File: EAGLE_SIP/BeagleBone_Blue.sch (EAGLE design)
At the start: 265 parts, among them M1 JST_ZH_2, M2 JST_ZH_2, M3 JST_ZH_2, M4 JST_ZH_2, P10 SCHA5B0200, Q3 MOSFET-N, U1 TPD4S012_DRY_6, U4 TPD4S012_DRY_6, U5 24LC_32AT-I/OT, U6 SN74LVC1G07_DCK_5, U7 TPS2051B_D_8, U8 MTFC4GLDEA, Y1 CM200C-32.768KAZF-UT, Y2 445C33D24M00000

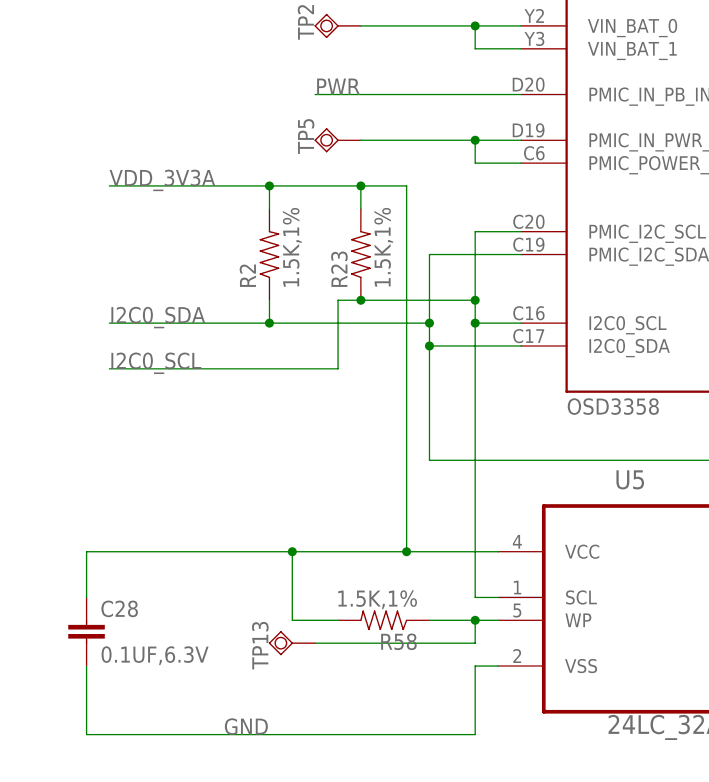
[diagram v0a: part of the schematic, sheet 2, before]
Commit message: Move U5 from VDD_3V3A to 3.3V
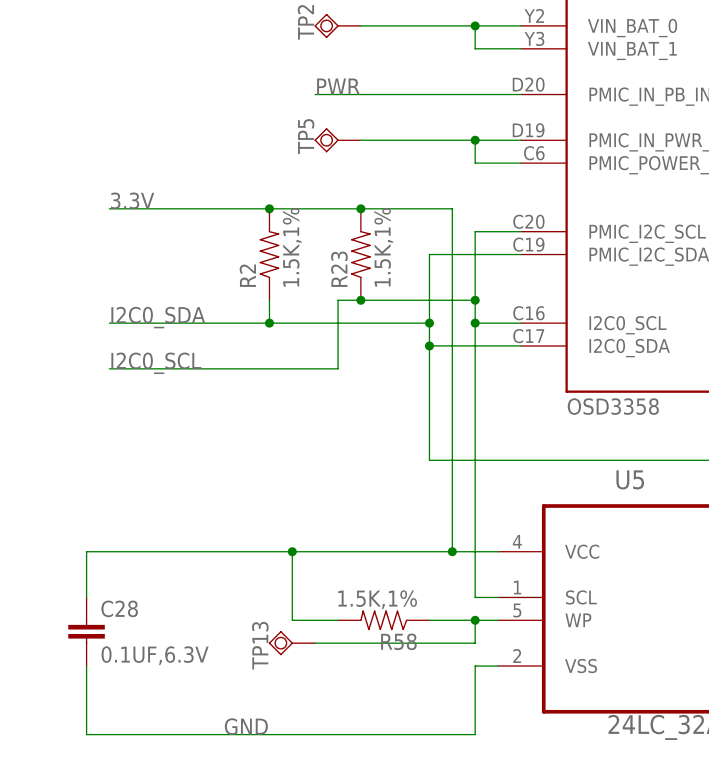
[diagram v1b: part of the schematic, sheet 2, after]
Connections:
- net 3.3V: now also C28.1, R2.2, R23.2, R58.2, U5.VCC
- net VDD_3V3A: no longer C28.1, R2.2, R23.2, R58.2, U5.VCC
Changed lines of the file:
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@@
 <net name="VDD_3V3A" class="0">
-<segment>
-<pinref part="R2" gate="G$1" pin="2"/>
-<wire x1="38.1" y1="203.2" x2="38.1" y2="205.74" width="0.1524" layer="91"/>
-<wire x1="20.32" y1="205.74" x2="38.1" y2="205.74" width="0.1524" layer="91"/>
-<pinref part="R23" gate="G$1" pin="2"/>
-<wire x1="38.1" y1="205.74" x2="48.26" y2="205.74" width="0.1524" layer="91"/>
-<wire x1="48.26" y1="205.74" x2="48.26" y2="203.2" width="0.1524" layer="91"/>
-<junction x="38.1" y="205.74"/>
-<label x="20.32" y="205.74" size="1.778" layer="95"/>
-<wire x1="48.26" y1="205.74" x2="53.34" y2="205.74" width="0.1524" layer="91"/>
-<junction x="48.26" y="205.74"/>
-<wire x1="53.34" y1="205.74" x2="53.34" y2="165.1" width="0.1524" layer="91"/>
-<pinref part="U5" gate="A" pin="VCC"/>
-<wire x1="53.34" y1="165.1" x2="63.5" y2="165.1" width="0.1524" layer="91"/>
-<wire x1="53.34" y1="165.1" x2="40.64" y2="165.1" width="0.1524" layer="91"/>
-<junction x="53.34" y="165.1"/>
-<wire x1="40.64" y1="165.1" x2="40.64" y2="157.48" width="0.1524" layer="91"/>
-<pinref part="R58" gate="G$1" pin="2"/>
-<wire x1="40.64" y1="157.48" x2="45.72" y2="157.48" width="0.1524" layer="91"/>
-<pinref part="C28" gate="G$1" pin="1"/>
-<wire x1="40.64" y1="165.1" x2="17.78" y2="165.1" width="0.1524" layer="91"/>
-<wire x1="17.78" y1="165.1" x2="17.78" y2="160.02" width="0.1524" layer="91"/>
-<junction x="40.64" y="165.1"/>
-</segment>
 <segment>
 <pinref part="R60" gate="G$1" pin="2"/>
@@
 <label x="236.22" y="210.82" size="1.778" layer="95"/>
 </segment>
+<segment>
+<pinref part="R58" gate="G$1" pin="2"/>
+<wire x1="40.64" y1="157.48" x2="45.72" y2="157.48" width="0.1524" layer="91"/>
+<pinref part="U5" gate="A" pin="VCC"/>
+<pinref part="C28" gate="G$1" pin="1"/>
+<wire x1="63.5" y1="165.1" x2="58.42" y2="165.1" width="0.1524" layer="91"/>
+<wire x1="58.42" y1="165.1" x2="40.64" y2="165.1" width="0.1524" layer="91"/>
+<wire x1="40.64" y1="165.1" x2="17.78" y2="165.1" width="0.1524" layer="91"/>
+<wire x1="17.78" y1="165.1" x2="17.78" y2="160.02" width="0.1524" layer="91"/>
+<wire x1="58.42" y1="165.1" x2="58.42" y2="203.2" width="0.1524" layer="91"/>
+<junction x="58.42" y="165.1"/>
+<pinref part="R23" gate="G$1" pin="2"/>
+<wire x1="58.42" y1="203.2" x2="48.26" y2="203.2" width="0.1524" layer="91"/>
+<pinref part="R2" gate="G$1" pin="2"/>
+<wire x1="38.1" y1="203.2" x2="48.26" y2="203.2" width="0.1524" layer="91"/>
+<junction x="48.26" y="203.2"/>
+<wire x1="38.1" y1="203.2" x2="20.32" y2="203.2" width="0.1524" layer="91"/>
+<junction x="38.1" y="203.2"/>
+<label x="20.32" y="203.2" size="1.778" layer="95"/>
+<wire x1="40.64" y1="157.48" x2="40.64" y2="165.1" width="0.1524" layer="91"/>
+<junction x="40.64" y="165.1"/>
+</segment>
 </net>

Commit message: Move U6 from VDD_3V3A to 3.3V
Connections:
- net 3.3V: now also R60.2
- net VDD_3V3A: no longer R60.2
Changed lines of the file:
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@@
-</segment>
-</net>
-<net name="VDD_3V3A" class="0">
-<segment>
-<pinref part="R60" gate="G$1" pin="2"/>
-<wire x1="274.32" y1="246.38" x2="274.32" y2="248.92" width="0.1524" layer="91"/>
-<wire x1="274.32" y1="248.92" x2="284.48" y2="248.92" width="0.1524" layer="91"/>
-<label x="284.48" y="248.92" size="1.778" layer="95"/>
 </segment>
 </net>
@@
 <junction x="40.64" y="165.1"/>
 </segment>
+<segment>
+<pinref part="R60" gate="G$1" pin="2"/>
+<wire x1="274.32" y1="246.38" x2="274.32" y2="248.92" width="0.1524" layer="91"/>
+<wire x1="274.32" y1="248.92" x2="292.1" y2="248.92" width="0.1524" layer="91"/>
+<label x="281.94" y="248.92" size="1.778" layer="95"/>
+</segment>
 </net>

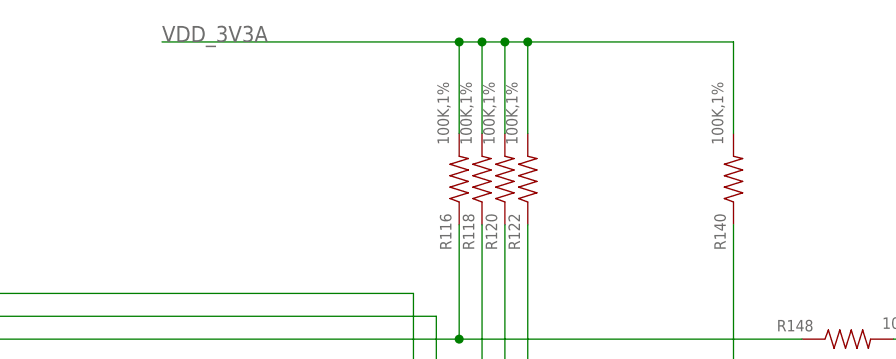
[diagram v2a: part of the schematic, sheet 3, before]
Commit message: Move pull-ups from VDD_3V3A to 3.3V
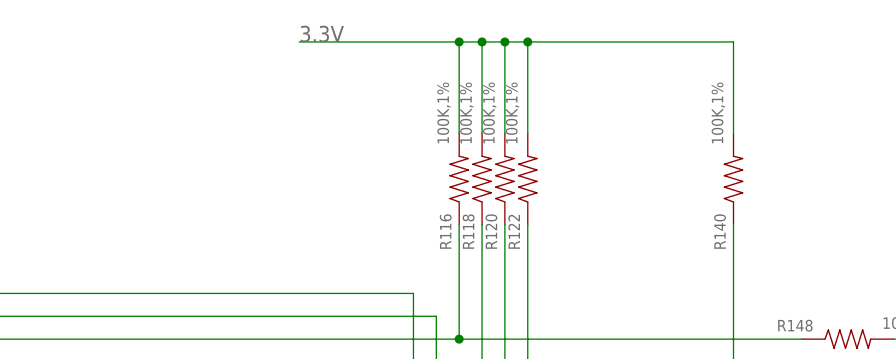
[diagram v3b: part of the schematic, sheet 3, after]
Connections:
- net 3.3V: now also R116.2, R120.2, R122.2, R140.2
- net VDD_3V3A: no longer R116.2, R118.2, R120.2, R122.2, R140.2
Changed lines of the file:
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@@
 <label x="55.88" y="177.8" size="1.778" layer="95"/>
+</segment>
+<segment>
+<pinref part="R140" gate="G$1" pin="2"/>
+<wire x1="297.18" y1="215.9" x2="297.18" y2="226.06" width="0.1524" layer="91"/>
+<wire x1="297.18" y1="226.06" x2="274.32" y2="226.06" width="0.1524" layer="91"/>
+<pinref part="R116" gate="G$1" pin="2"/>
+<wire x1="274.32" y1="226.06" x2="271.78" y2="226.06" width="0.1524" layer="91"/>
+<wire x1="271.78" y1="226.06" x2="269.24" y2="226.06" width="0.1524" layer="91"/>
+<wire x1="269.24" y1="226.06" x2="266.7" y2="226.06" width="0.1524" layer="91"/>
+<wire x1="266.7" y1="226.06" x2="248.92" y2="226.06" width="0.1524" layer="91"/>
+<wire x1="266.7" y1="215.9" x2="266.7" y2="226.06" width="0.1524" layer="91"/>
+<junction x="266.7" y="226.06"/>
+<wire x1="269.24" y1="215.9" x2="269.24" y2="226.06" width="0.1524" layer="91"/>
+<junction x="269.24" y="226.06"/>
+<pinref part="R120" gate="G$1" pin="2"/>
+<wire x1="271.78" y1="215.9" x2="271.78" y2="226.06" width="0.1524" layer="91"/>
+<junction x="271.78" y="226.06"/>
+<pinref part="R122" gate="G$1" pin="2"/>
+<wire x1="274.32" y1="215.9" x2="274.32" y2="226.06" width="0.1524" layer="91"/>
+<junction x="274.32" y="226.06"/>
+<label x="248.92" y="226.06" size="1.778" layer="95"/>
 </segment>
 </net>
@@
 <net name="VDD_3V3A" class="0">
 <segment>
-<wire x1="233.68" y1="226.06" x2="266.7" y2="226.06" width="0.1524" layer="91"/>
-<pinref part="R140" gate="G$1" pin="2"/>
-<wire x1="297.18" y1="226.06" x2="297.18" y2="215.9" width="0.1524" layer="91"/>
-<pinref part="R116" gate="G$1" pin="2"/>
-<wire x1="266.7" y1="226.06" x2="269.24" y2="226.06" width="0.1524" layer="91"/>
-<wire x1="269.24" y1="226.06" x2="271.78" y2="226.06" width="0.1524" layer="91"/>
-<wire x1="271.78" y1="226.06" x2="274.32" y2="226.06" width="0.1524" layer="91"/>
-<wire x1="274.32" y1="226.06" x2="297.18" y2="226.06" width="0.1524" layer="91"/>
-<wire x1="266.7" y1="226.06" x2="266.7" y2="215.9" width="0.1524" layer="91"/>
-<junction x="266.7" y="226.06"/>
-<pinref part="R118" gate="G$1" pin="2"/>
-<wire x1="269.24" y1="226.06" x2="269.24" y2="215.9" width="0.1524" layer="91"/>
-<junction x="269.24" y="226.06"/>
-<pinref part="R120" gate="G$1" pin="2"/>
-<wire x1="271.78" y1="226.06" x2="271.78" y2="215.9" width="0.1524" layer="91"/>
-<junction x="271.78" y="226.06"/>
-<pinref part="R122" gate="G$1" pin="2"/>
-<wire x1="274.32" y1="226.06" x2="274.32" y2="215.9" width="0.1524" layer="91"/>
-<junction x="274.32" y="226.06"/>
-<label x="233.68" y="226.06" size="1.778" layer="95"/>
-</segment>
-<segment>
 <pinref part="R157" gate="G$1" pin="1"/>

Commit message: Move pull-ups from VDD_3V3A to 3.3V
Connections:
- net 3.3V: now also R118.2
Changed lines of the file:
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@@
 <wire x1="266.7" y1="215.9" x2="266.7" y2="226.06" width="0.1524" layer="91"/>
 <junction x="266.7" y="226.06"/>
-<wire x1="269.24" y1="215.9" x2="269.24" y2="226.06" width="0.1524" layer="91"/>
-<junction x="269.24" y="226.06"/>
 <pinref part="R120" gate="G$1" pin="2"/>
 <wire x1="271.78" y1="215.9" x2="271.78" y2="226.06" width="0.1524" layer="91"/>
@@
 <junction x="274.32" y="226.06"/>
 <label x="248.92" y="226.06" size="1.778" layer="95"/>
+<pinref part="R118" gate="G$1" pin="2"/>
+<wire x1="269.24" y1="215.9" x2="269.24" y2="226.06" width="0.1524" layer="91"/>
+<junction x="269.24" y="226.06"/>
 </segment>
 </net>

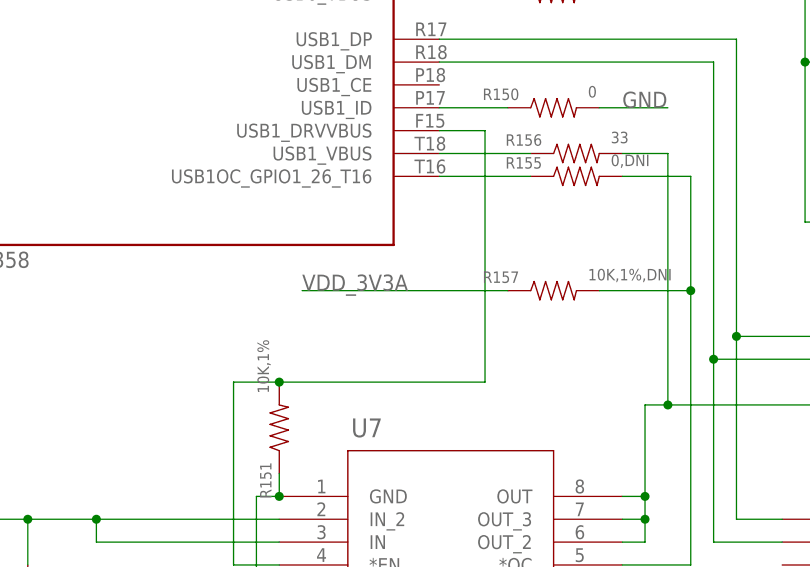
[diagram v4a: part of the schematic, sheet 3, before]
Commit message: Move pull-ups from VDD_3V3A to 3.3V
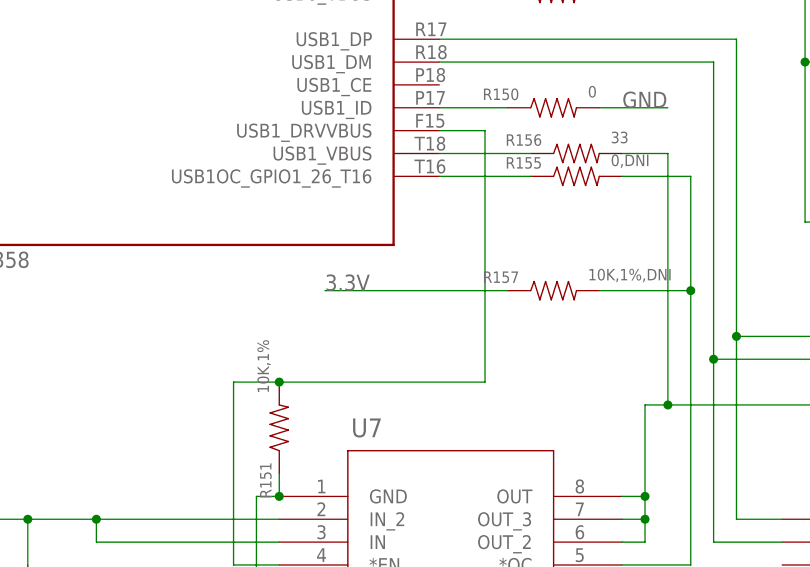
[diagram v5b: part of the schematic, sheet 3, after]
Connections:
- net 3.3V: now also R157.1
- net VDD_3V3A: no longer R157.1
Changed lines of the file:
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@@
 <junction x="269.24" y="226.06"/>
+</segment>
+<segment>
+<pinref part="R157" gate="G$1" pin="1"/>
+<wire x1="198.12" y1="93.98" x2="177.8" y2="93.98" width="0.1524" layer="91"/>
+<label x="177.8" y="93.98" size="1.778" layer="95"/>
 </segment>
 </net>
@@
 </segment>
 </net>
-<net name="VDD_3V3A" class="0">
-<segment>
-<pinref part="R157" gate="G$1" pin="1"/>
-<wire x1="198.12" y1="93.98" x2="175.26" y2="93.98" width="0.1524" layer="91"/>
-<label x="175.26" y="93.98" size="1.778" layer="95"/>
-</segment>
-</net>

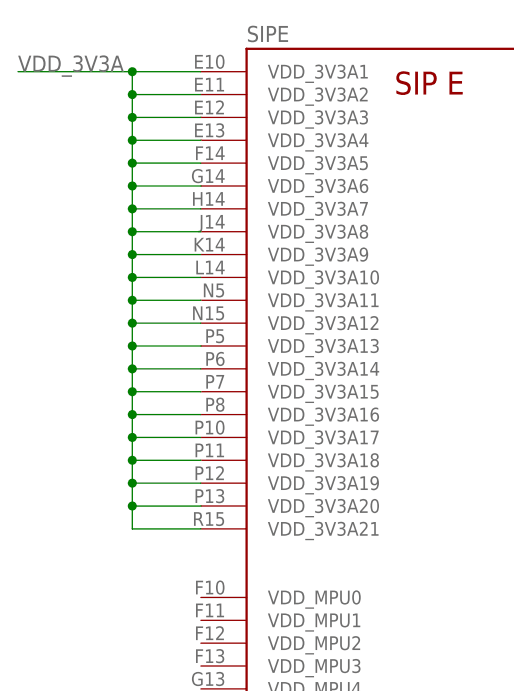
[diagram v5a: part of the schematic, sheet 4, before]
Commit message: Remove unused VDD_3V3A
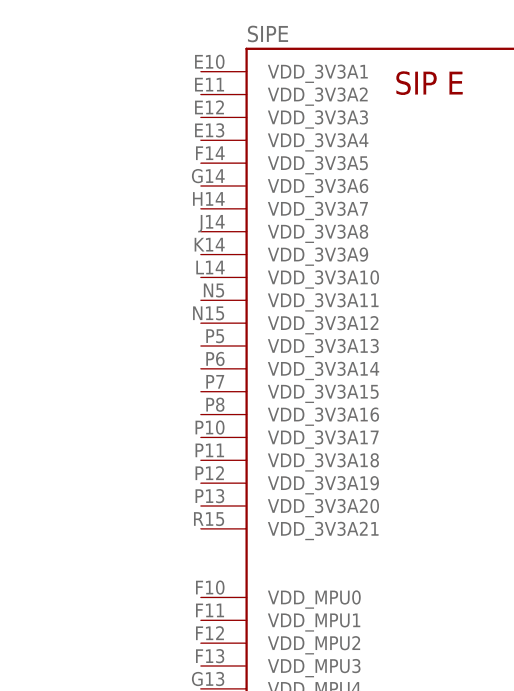
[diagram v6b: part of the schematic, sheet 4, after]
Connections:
- removed net VDD_3V3A: SIPE.VDD_3V3A1, SIPE.VDD_3V3A10, SIPE.VDD_3V3A11, SIPE.VDD_3V3A12, SIPE.VDD_3V3A13, SIPE.VDD_3V3A14, SIPE.VDD_3V3A15, SIPE.VDD_3V3A16, SIPE.VDD_3V3A17, SIPE.VDD_3V3A18, SIPE.VDD_3V3A19, SIPE.VDD_3V3A2, SIPE.VDD_3V3A20, SIPE.VDD_3V3A21, SIPE.VDD_3V3A3, SIPE.VDD_3V3A4, SIPE.VDD_3V3A5, SIPE.VDD_3V3A6, SIPE.VDD_3V3A7, SIPE.VDD_3V3A8, SIPE.VDD_3V3A9
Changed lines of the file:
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@@
-</segment>
-</net>
-<net name="VDD_3V3A" class="0">
-<segment>
-<pinref part="SIP" gate="E" pin="VDD_3V3A1"/>
-<wire x1="53.34" y1="226.06" x2="66.04" y2="226.06" width="0.1524" layer="91"/>
-<pinref part="SIP" gate="E" pin="VDD_3V3A2"/>
-<wire x1="66.04" y1="226.06" x2="73.66" y2="226.06" width="0.1524" layer="91"/>
-<wire x1="73.66" y1="223.52" x2="66.04" y2="223.52" width="0.1524" layer="91"/>
-<wire x1="66.04" y1="223.52" x2="66.04" y2="226.06" width="0.1524" layer="91"/>
-<junction x="66.04" y="226.06"/>
-<pinref part="SIP" gate="E" pin="VDD_3V3A3"/>
-<wire x1="73.66" y1="220.98" x2="66.04" y2="220.98" width="0.1524" layer="91"/>
-<wire x1="66.04" y1="220.98" x2="66.04" y2="223.52" width="0.1524" layer="91"/>
-<junction x="66.04" y="223.52"/>
-<pinref part="SIP" gate="E" pin="VDD_3V3A4"/>
-<wire x1="73.66" y1="218.44" x2="66.04" y2="218.44" width="0.1524" layer="91"/>
-<wire x1="66.04" y1="218.44" x2="66.04" y2="220.98" width="0.1524" layer="91"/>
-<junction x="66.04" y="220.98"/>
-<pinref part="SIP" gate="E" pin="VDD_3V3A5"/>
-<wire x1="73.66" y1="215.9" x2="66.04" y2="215.9" width="0.1524" layer="91"/>
-<wire x1="66.04" y1="215.9" x2="66.04" y2="218.44" width="0.1524" layer="91"/>
-<junction x="66.04" y="218.44"/>
-<pinref part="SIP" gate="E" pin="VDD_3V3A6"/>
-<wire x1="73.66" y1="213.36" x2="66.04" y2="213.36" width="0.1524" layer="91"/>
-<wire x1="66.04" y1="213.36" x2="66.04" y2="215.9" width="0.1524" layer="91"/>
-<junction x="66.04" y="215.9"/>
-<pinref part="SIP" gate="E" pin="VDD_3V3A7"/>
-<wire x1="73.66" y1="210.82" x2="66.04" y2="210.82" width="0.1524" layer="91"/>
-<wire x1="66.04" y1="210.82" x2="66.04" y2="213.36" width="0.1524" layer="91"/>
-<junction x="66.04" y="213.36"/>
-<pinref part="SIP" gate="E" pin="VDD_3V3A8"/>
-<wire x1="73.66" y1="208.28" x2="66.04" y2="208.28" width="0.1524" layer="91"/>
-<wire x1="66.04" y1="208.28" x2="66.04" y2="210.82" width="0.1524" layer="91"/>
-<junction x="66.04" y="210.82"/>
-<pinref part="SIP" gate="E" pin="VDD_3V3A9"/>
-<wire x1="73.66" y1="205.74" x2="66.04" y2="205.74" width="0.1524" layer="91"/>
-<wire x1="66.04" y1="205.74" x2="66.04" y2="208.28" width="0.1524" layer="91"/>
-<junction x="66.04" y="208.28"/>
-<pinref part="SIP" gate="E" pin="VDD_3V3A10"/>
-<wire x1="73.66" y1="203.2" x2="66.04" y2="203.2" width="0.1524" layer="91"/>
-<wire x1="66.04" y1="203.2" x2="66.04" y2="205.74" width="0.1524" layer="91"/>
-<junction x="66.04" y="205.74"/>
-<pinref part="SIP" gate="E" pin="VDD_3V3A11"/>
-<wire x1="73.66" y1="200.66" x2="66.04" y2="200.66" width="0.1524" layer="91"/>
-<wire x1="66.04" y1="200.66" x2="66.04" y2="203.2" width="0.1524" layer="91"/>
-<junction x="66.04" y="203.2"/>
-<pinref part="SIP" gate="E" pin="VDD_3V3A12"/>
-<wire x1="73.66" y1="198.12" x2="66.04" y2="198.12" width="0.1524" layer="91"/>
-<wire x1="66.04" y1="198.12" x2="66.04" y2="200.66" width="0.1524" layer="91"/>
-<junction x="66.04" y="200.66"/>
-<pinref part="SIP" gate="E" pin="VDD_3V3A13"/>
-<wire x1="73.66" y1="195.58" x2="66.04" y2="195.58" width="0.1524" layer="91"/>
-<wire x1="66.04" y1="195.58" x2="66.04" y2="198.12" width="0.1524" layer="91"/>
-<junction x="66.04" y="198.12"/>
-<pinref part="SIP" gate="E" pin="VDD_3V3A14"/>
-<wire x1="73.66" y1="193.04" x2="66.04" y2="193.04" width="0.1524" layer="91"/>
-<wire x1="66.04" y1="193.04" x2="66.04" y2="195.58" width="0.1524" layer="91"/>
-<junction x="66.04" y="195.58"/>
-<pinref part="SIP" gate="E" pin="VDD_3V3A15"/>
-<wire x1="73.66" y1="190.5" x2="66.04" y2="190.5" width="0.1524" layer="91"/>
-<wire x1="66.04" y1="190.5" x2="66.04" y2="193.04" width="0.1524" layer="91"/>
-<junction x="66.04" y="193.04"/>
-<pinref part="SIP" gate="E" pin="VDD_3V3A16"/>
-<wire x1="73.66" y1="187.96" x2="66.04" y2="187.96" width="0.1524" layer="91"/>
-<wire x1="66.04" y1="187.96" x2="66.04" y2="190.5" width="0.1524" layer="91"/>
-<junction x="66.04" y="190.5"/>
-<pinref part="SIP" gate="E" pin="VDD_3V3A17"/>
-<wire x1="73.66" y1="185.42" x2="66.04" y2="185.42" width="0.1524" layer="91"/>
-<wire x1="66.04" y1="185.42" x2="66.04" y2="187.96" width="0.1524" layer="91"/>
-<junction x="66.04" y="187.96"/>
-<pinref part="SIP" gate="E" pin="VDD_3V3A18"/>
-<wire x1="73.66" y1="182.88" x2="66.04" y2="182.88" width="0.1524" layer="91"/>
-<wire x1="66.04" y1="182.88" x2="66.04" y2="185.42" width="0.1524" layer="91"/>
-<junction x="66.04" y="185.42"/>
-<pinref part="SIP" gate="E" pin="VDD_3V3A19"/>
-<wire x1="73.66" y1="180.34" x2="66.04" y2="180.34" width="0.1524" layer="91"/>
-<wire x1="66.04" y1="180.34" x2="66.04" y2="182.88" width="0.1524" layer="91"/>
-<junction x="66.04" y="182.88"/>
-<pinref part="SIP" gate="E" pin="VDD_3V3A20"/>
-<wire x1="73.66" y1="177.8" x2="66.04" y2="177.8" width="0.1524" layer="91"/>
-<wire x1="66.04" y1="177.8" x2="66.04" y2="180.34" width="0.1524" layer="91"/>
-<junction x="66.04" y="180.34"/>
-<pinref part="SIP" gate="E" pin="VDD_3V3A21"/>
-<wire x1="73.66" y1="175.26" x2="66.04" y2="175.26" width="0.1524" layer="91"/>
-<wire x1="66.04" y1="175.26" x2="66.04" y2="177.8" width="0.1524" layer="91"/>
-<junction x="66.04" y="177.8"/>
-<label x="53.34" y="226.06" size="1.778" layer="95"/>
 </segment>
 </net>
